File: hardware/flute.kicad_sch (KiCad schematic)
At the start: 16 parts, among them J1 AudioJack2, J2 Conn_01x02, SW1 C, SW2 D, SW3 E, SW4 F, SW5 G, SW6 A, SW7 H, SW8 OCTAVE?

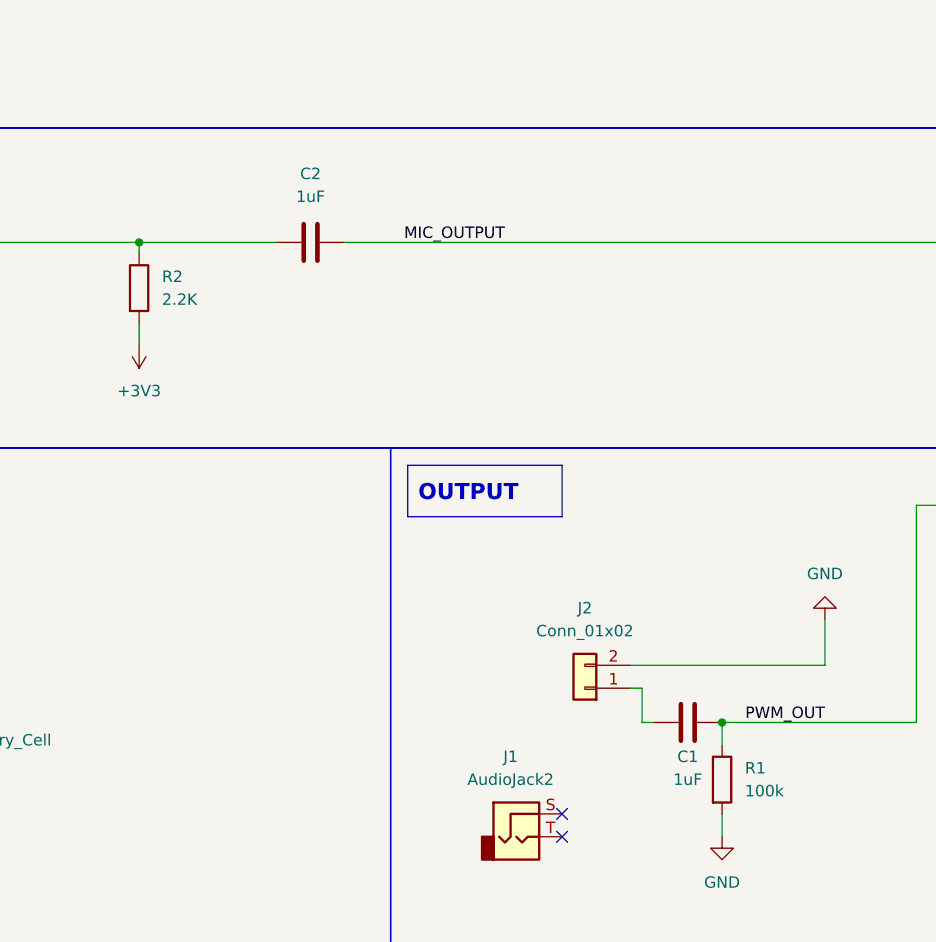
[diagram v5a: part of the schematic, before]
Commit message: test points added to the schematic
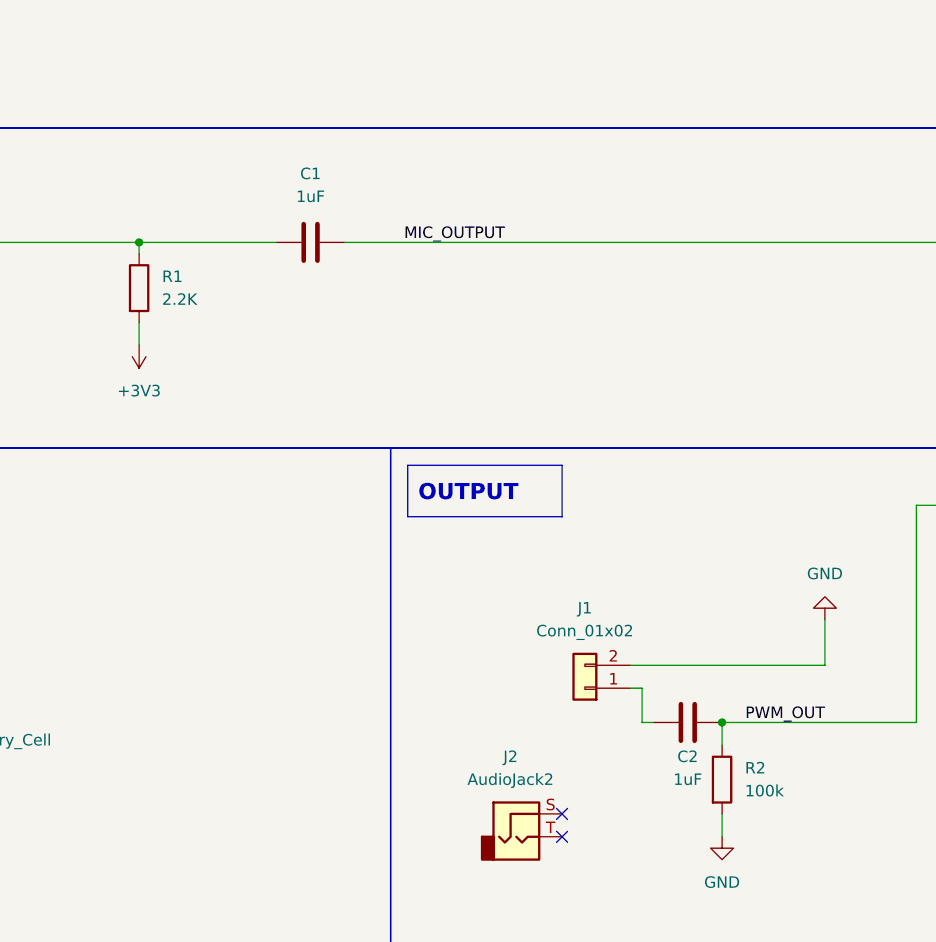
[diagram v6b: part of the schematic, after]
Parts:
- renumbered C2 to C1, C1 to C2, J2 to J1, J1 to J2, R2 to R1, R1 to R2
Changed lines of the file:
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@@
 		(dnp no)
 		(fields_autoplaced yes)
-		(property "Reference" "#PWR06"
+		(property "Reference" "#PWR03"
 			(at 62.23 134.62 0)
 			(effects
@@
 			(project "flute"
 				(path "/9ae53f79-8ce2-4a44-ba8e-dca375125c34"
-					(reference "#PWR06")
+					(reference "#PWR03")
 					(unit 1)
 				)
@@
 		(dnp no)
 		(fields_autoplaced yes)
-		(property "Reference" "J2"
+		(property "Reference" "J1"
 			(at 132.08 156.21 0)
 			(effects
@@
 			(project ""
 				(path "/9ae53f79-8ce2-4a44-ba8e-dca375125c34"
-					(reference "J2")
+					(reference "J1")
 					(unit 1)
 				)
@@
 		(dnp no)
 		(fields_autoplaced yes)
-		(property "Reference" "R1"
+		(property "Reference" "R2"
 			(at 149.86 173.9899 0)
 			(effects
@@
 			(project "flute"
 				(path "/9ae53f79-8ce2-4a44-ba8e-dca375125c34"
-					(reference "R1")
+					(reference "R2")
 					(unit 1)
 				)
@@
 		(dnp no)
 		(fields_autoplaced yes)
-		(property "Reference" "#PWR05"
+		(property "Reference" "#PWR01"
 			(at 62.23 91.44 0)
 			(effects
@@
 			(project "flute"
 				(path "/9ae53f79-8ce2-4a44-ba8e-dca375125c34"
-					(reference "#PWR05")
+					(reference "#PWR01")
 					(unit 1)
 				)
@@
 		(dnp no)
 		(fields_autoplaced yes)
-		(property "Reference" "#PWR01"
+		(property "Reference" "#PWR05"
 			(at 58.42 166.37 0)
 			(effects
@@
 			(project ""
 				(path "/9ae53f79-8ce2-4a44-ba8e-dca375125c34"
-					(reference "#PWR01")
+					(reference "#PWR05")
 					(unit 1)
 				)
@@
 		(dnp no)
 		(fields_autoplaced yes)
-		(property "Reference" "#PWR03"
+		(property "Reference" "#PWR07"
 			(at 147.32 187.96 0)
 			(effects
@@
 			(project "flute"
 				(path "/9ae53f79-8ce2-4a44-ba8e-dca375125c34"
-					(reference "#PWR03")
+					(reference "#PWR07")
 					(unit 1)
 				)
@@
 		(dnp no)
 		(fields_autoplaced yes)
-		(property "Reference" "J1"
+		(property "Reference" "J2"
 			(at 123.825 172.72 0)
 			(effects
@@
 			(project ""
 				(path "/9ae53f79-8ce2-4a44-ba8e-dca375125c34"
-					(reference "J1")
+					(reference "J2")
 					(unit 1)
 				)
@@
 		(dnp no)
 		(fields_autoplaced yes)
-		(property "Reference" "C2"
+		(property "Reference" "C1"
 			(at 101.6 107.95 90)
 			(effects
@@
 			(project "flute"
 				(path "/9ae53f79-8ce2-4a44-ba8e-dca375125c34"
-					(reference "C2")
+					(reference "C1")
 					(unit 1)
 				)
@@
 		(dnp no)
 		(fields_autoplaced yes)
-		(property "Reference" "#PWR07"
+		(property "Reference" "#PWR02"
 			(at 82.55 123.19 0)
 			(effects
@@
 			(project "flute"
 				(path "/9ae53f79-8ce2-4a44-ba8e-dca375125c34"
-					(reference "#PWR07")
+					(reference "#PWR02")
 					(unit 1)
 				)
@@
 		(dnp no)
 		(fields_autoplaced yes)
-		(property "Reference" "R2"
+		(property "Reference" "R1"
 			(at 85.09 119.3799 0)
 			(effects
@@
 			(project "flute"
 				(path "/9ae53f79-8ce2-4a44-ba8e-dca375125c34"
-					(reference "R2")
+					(reference "R1")
 					(unit 1)
 				)
@@
 		(dnp no)
 		(fields_autoplaced yes)
-		(property "Reference" "#PWR02"
+		(property "Reference" "#PWR06"
 			(at 58.42 185.42 0)
 			(effects
@@
 			(project ""
 				(path "/9ae53f79-8ce2-4a44-ba8e-dca375125c34"
-					(reference "#PWR02")
+					(reference "#PWR06")
 					(unit 1)
 				)
@@
 		(on_board yes)
 		(dnp no)
-		(property "Reference" "C1"
+		(property "Reference" "C2"
 			(at 143.51 172.72 90)
 			(effects
@@
 			(project "flute"
 				(path "/9ae53f79-8ce2-4a44-ba8e-dca375125c34"
-					(reference "C1")
-					(unit 1)
-				)
+					(reference "C2")
+					(unit 1)
+				)

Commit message: test points placed on the pcb
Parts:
- added TP?: TestPoint, TestPoint:TestPoint_Bridge_Pitch2.54mm_Drill1.3mm, symbol Connector:TestPoint
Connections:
- net PWM_OUT: now also TP?.1
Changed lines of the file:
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@@
+	)
+	(junction
+		(at 154.94 168.91)
+		(diameter 0)
+		(color 0 0 0 0)
 	)
 	(junction
@@
 	)
 	(junction
+		(at 62.23 57.15)
+		(diameter 0)
+		(color 0 0 0 0)
+	)
+	(junction
 		(at 147.32 168.91)
 		(diameter 0)
 		(color 0 0 0 0)
 	)
-	(junction
-		(at 62.23 57.15)
-		(diameter 0)
-		(color 0 0 0 0)
-	)
 	(no_connect
 		(at 261.62 63.5)
@@
 	(wire
 		(pts
+			(xy 147.32 168.91) (xy 154.94 168.91)
+		)
+		(stroke
+			(width 0)
+			(type default)
+		)
+	)
+	(wire
+		(pts
 			(xy 62.23 82.55) (xy 62.23 85.09)
 		)
@@
 	(wire
 		(pts
+			(xy 154.94 168.91) (xy 168.91 168.91)
+		)
+		(stroke
+			(width 0)
+			(type default)
+		)
+	)
+	(wire
+		(pts
 			(xy 62.23 115.57) (xy 82.55 115.57)
 		)
@@
 		(pts
 			(xy 77.47 38.1) (xy 62.23 38.1)
-		)
-		(stroke
-			(width 0)
-			(type default)
-		)
-	)
-	(wire
-		(pts
-			(xy 147.32 168.91) (xy 168.91 168.91)
 		)
 		(stroke
@@
 					(unit 1)
 				)
+			)
+		)
+	)
+	(symbol
+		(lib_id "Connector:TestPoint")
+		(at 154.94 168.91 90)
+		(unit 1)
+		(exclude_from_sim no)
+		(in_bom yes)
+		(on_board yes)
+		(dnp no)
+		(fields_autoplaced yes)
+		(property "Reference" "TP?"
+			(at 151.638 163.83 90)
+			(effects
+				(font
+					(size 1.27 1.27)
+				)
+			)
+		)
+		(property "Value" "TestPoint"
+			(at 151.638 166.37 90)
+			(effects
+				(font
+					(size 1.27 1.27)
+				)
+			)
+		)
+		(property "Footprint" "TestPoint:TestPoint_Bridge_Pitch2.54mm_Drill1.3mm"
+			(at 154.94 163.83 0)
+			(effects
+				(font
+					(size 1.27 1.27)
+				)
+				(hide yes)
+			)
+		)
+		(property "Datasheet" "~"
+			(at 154.94 163.83 0)
+			(effects
+				(font
+					(size 1.27 1.27)
+				)
+				(hide yes)
+			)
+		)
+		(property "Description" "test point"
+			(at 154.94 168.91 0)
+			(effects
+				(font
+					(size 1.27 1.27)
+				)
+				(hide yes)
+			)
+		)
+		(pin "1"
+		)
+		(instances
+			(project ""
+				(path "/9ae53f79-8ce2-4a44-ba8e-dca375125c34"
+					(reference "TP?")
+					(unit 1)
+				)

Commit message: saved changes
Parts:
- gave numbers to parts that had none: 1
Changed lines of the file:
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@@
 		(dnp no)
 		(fields_autoplaced yes)
-		(property "Reference" "TP?"
+		(property "Reference" "TP1"
 			(at 151.638 163.83 90)
 			(effects
@@
 			(project ""
 				(path "/9ae53f79-8ce2-4a44-ba8e-dca375125c34"
-					(reference "TP?")
+					(reference "TP1")
 					(unit 1)
 				)
